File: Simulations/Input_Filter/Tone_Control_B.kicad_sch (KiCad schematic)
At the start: 11 parts, among them U17 TL072

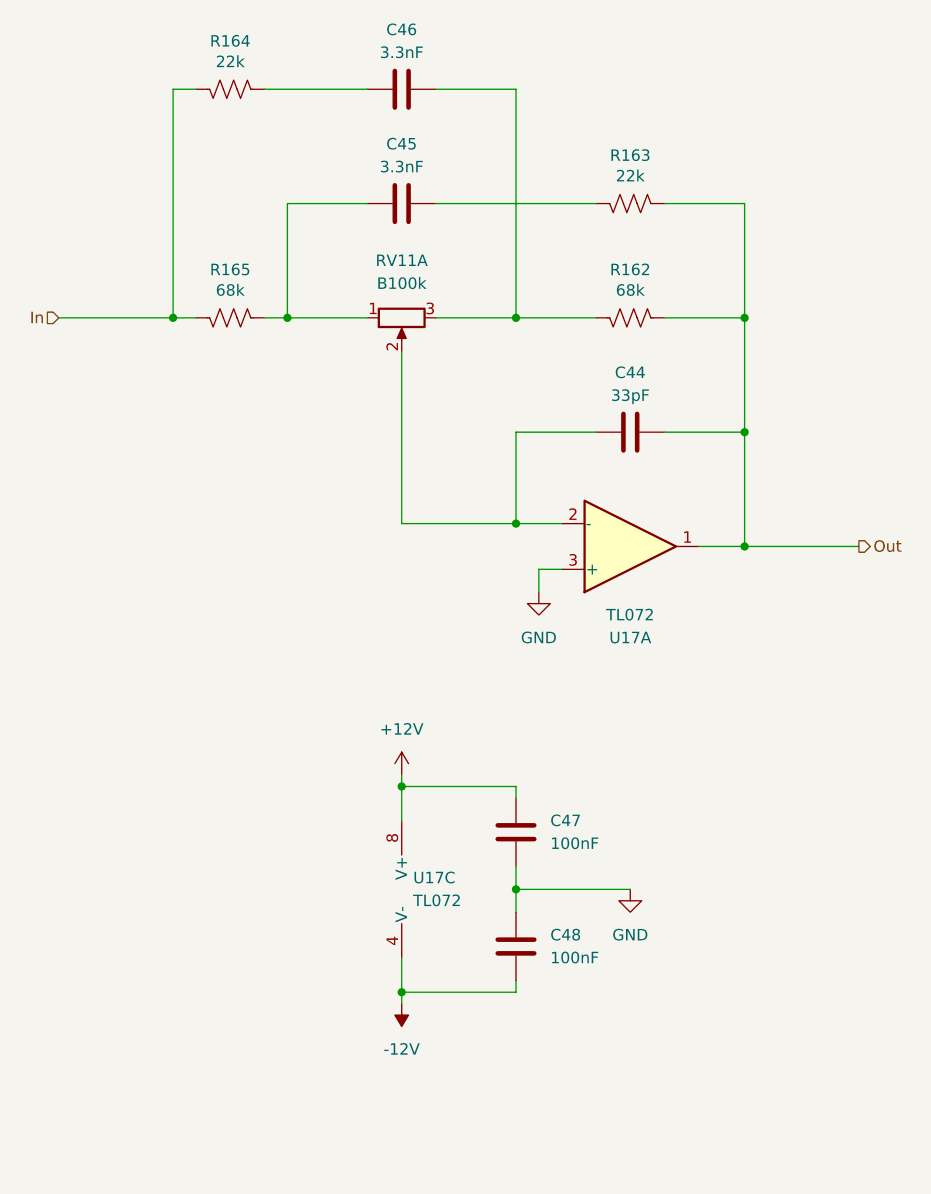
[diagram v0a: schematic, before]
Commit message: Scaled up components in Tone Control part
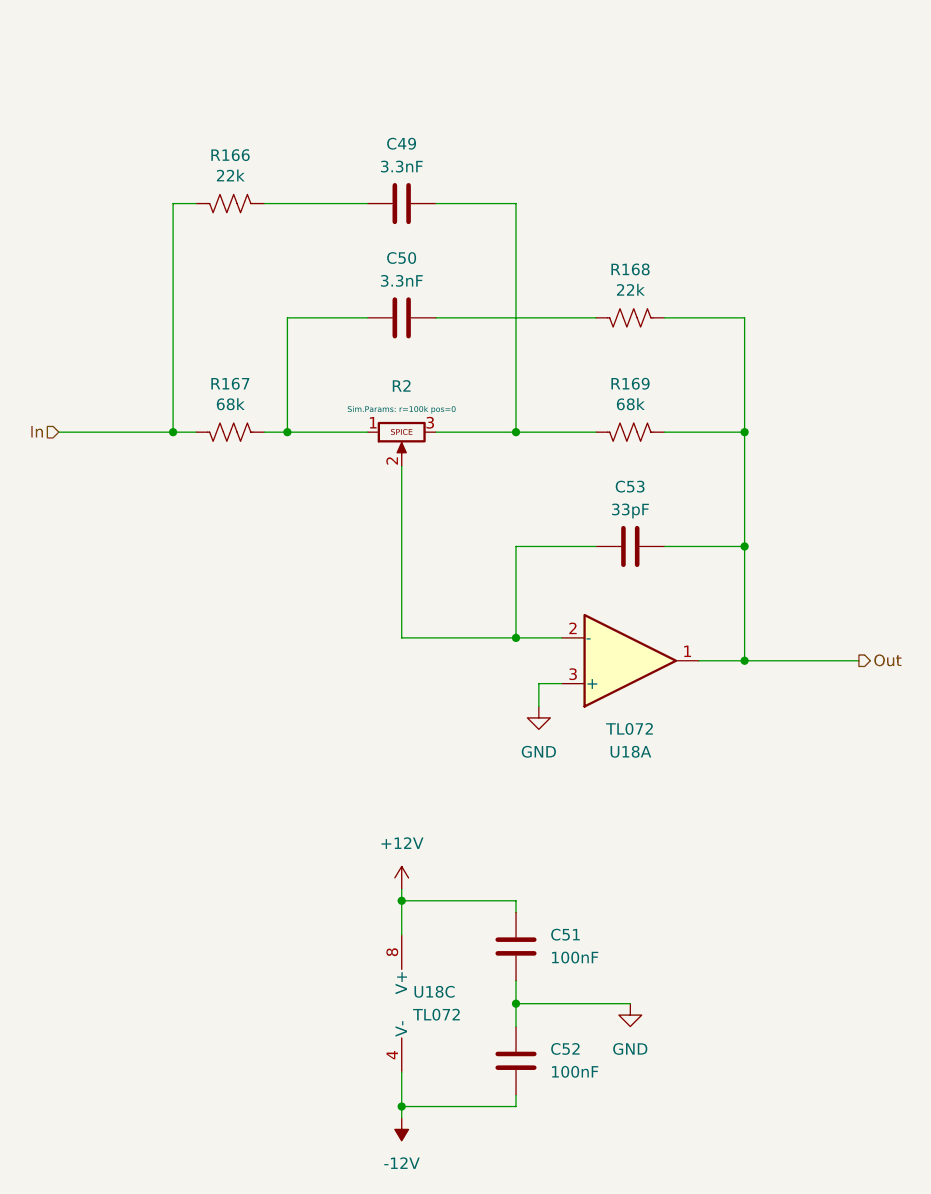
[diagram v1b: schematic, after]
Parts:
- removed C44: 33pF, Capacitor_THT:C_Disc_D3.0mm_W2.0mm_P2.50mm, symbol Device:C
- removed C45, C46: 3.3nF, Capacitor_THT:C_Disc_D4.3mm_W1.9mm_P5.00mm, symbol Device:C
- removed C47, C48: 100nF, Capacitor_THT:C_Disc_D4.3mm_W1.9mm_P5.00mm, symbol Device:C
- removed R162, R165: 68k, Resistor_THT:R_Axial_DIN0207_L6.3mm_D2.5mm_P7.62mm_Horizontal, symbol Device:R_US
- removed R163, R164: 22k, Resistor_THT:R_Axial_DIN0207_L6.3mm_D2.5mm_P7.62mm_Horizontal, symbol Device:R_US
- removed RV11: B100k, Potentiometer_THT:Potentiometer_Alps_RK09L_Double_Vertical, symbol Device:R_Potentiometer_Dual_Separate
- removed U17: TL072, Package_DIP:DIP-8_W7.62mm_Socket, symbol Amplifier_Operational:TL072
- added C49, C50: 3.3nF, Capacitor_THT:C_Disc_D4.3mm_W1.9mm_P5.00mm, symbol Device:C
- added C51, C52: 100nF, Capacitor_THT:C_Disc_D4.3mm_W1.9mm_P5.00mm, symbol Device:C
- added C53: 33pF, Capacitor_THT:C_Disc_D3.0mm_W2.0mm_P2.50mm, symbol Device:C
- added R166, R168: 22k, Resistor_THT:R_Axial_DIN0207_L6.3mm_D2.5mm_P7.62mm_Horizontal, symbol Device:R_US
- added R167, R169: 68k, Resistor_THT:R_Axial_DIN0207_L6.3mm_D2.5mm_P7.62mm_Horizontal, symbol Device:R_US
- added R2: Potentiometer, symbol Simulation_SPICE:Potentiometer
- added U18: TL072, Package_DIP:DIP-8_W7.62mm_Socket, symbol Amplifier_Operational:TL072
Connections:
- net +12V: now also C51.1, U18.8 (V+)
- net -12V: now also C52.2, U18.4 (V-)
- net GND: now also C51.2, C52.1, U18.3 (+)
- net In: now also R166.1, R167.1
- net Out: now also C53.2, R168.2, R169.2, U18.1
- new net: C49.1, R166.2
- new net: C53.1, R2.2, U18.2 (-)
- new net: C49.2, R169.1, R2.3
- new net: C50.1, R167.2, R2.1
- new net: C50.2, R168.1
